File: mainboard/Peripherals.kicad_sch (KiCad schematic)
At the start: 37 parts, among them IC1101 PCAL6416AHF, IC1102 TMP117xxYBG, IC1103 PCA9306JK, IC1104 PCA9633DP1,118, IC1105 RV-8263-C8, Q1101 DMN2053UQ, Q1102 DMN2053UQ

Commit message: Feature: Issue #18
- Replace XPGDWT-BS-0000-00Q2E with XPGDWT-BS-0000-00P5E
- Update CHANGELOG with previous commits

Closes: #18

Signed-off-by: Daniel Kampert <DanielKampert@kampis-elektroecke.de>

Signed-off-by: Daniel Kampert <DanielKampert@kampis-elektroecke.de>
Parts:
- D1101, D1102: manf# XPGDWT-BS-0000-00Q2E -> XPGDWT-BS-0000-00P5E; mouser# 941-PGDWTBS000000Q2E -> 941-XPGDWT-BS-0000-00P5E
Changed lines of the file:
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@@
 			)
 		)
-		(property "manf#" "XPGDWT-BS-0000-00Q2E"
+		(property "manf#" "XPGDWT-BS-0000-00P5E"
 			(at 187.96 102.87 0)
 			(effects
@@
 			)
 		)
-		(property "mouser#" "941-PGDWTBS000000Q2E"
+		(property "mouser#" "941-XPGDWT-BS-0000-00P5E"
 			(at 187.96 102.87 0)
 			(effects
@@
 			)
 		)
-		(property "manf#" "XPGDWT-BS-0000-00Q2E"
+		(property "manf#" "XPGDWT-BS-0000-00P5E"
 			(at 227.33 102.87 0)
 			(effects
@@
 			)
 		)
-		(property "mouser#" "941-PGDWTBS000000Q2E"
+		(property "mouser#" "941-XPGDWT-BS-0000-00P5E"
 			(at 227.33 102.87 0)
 			(effects

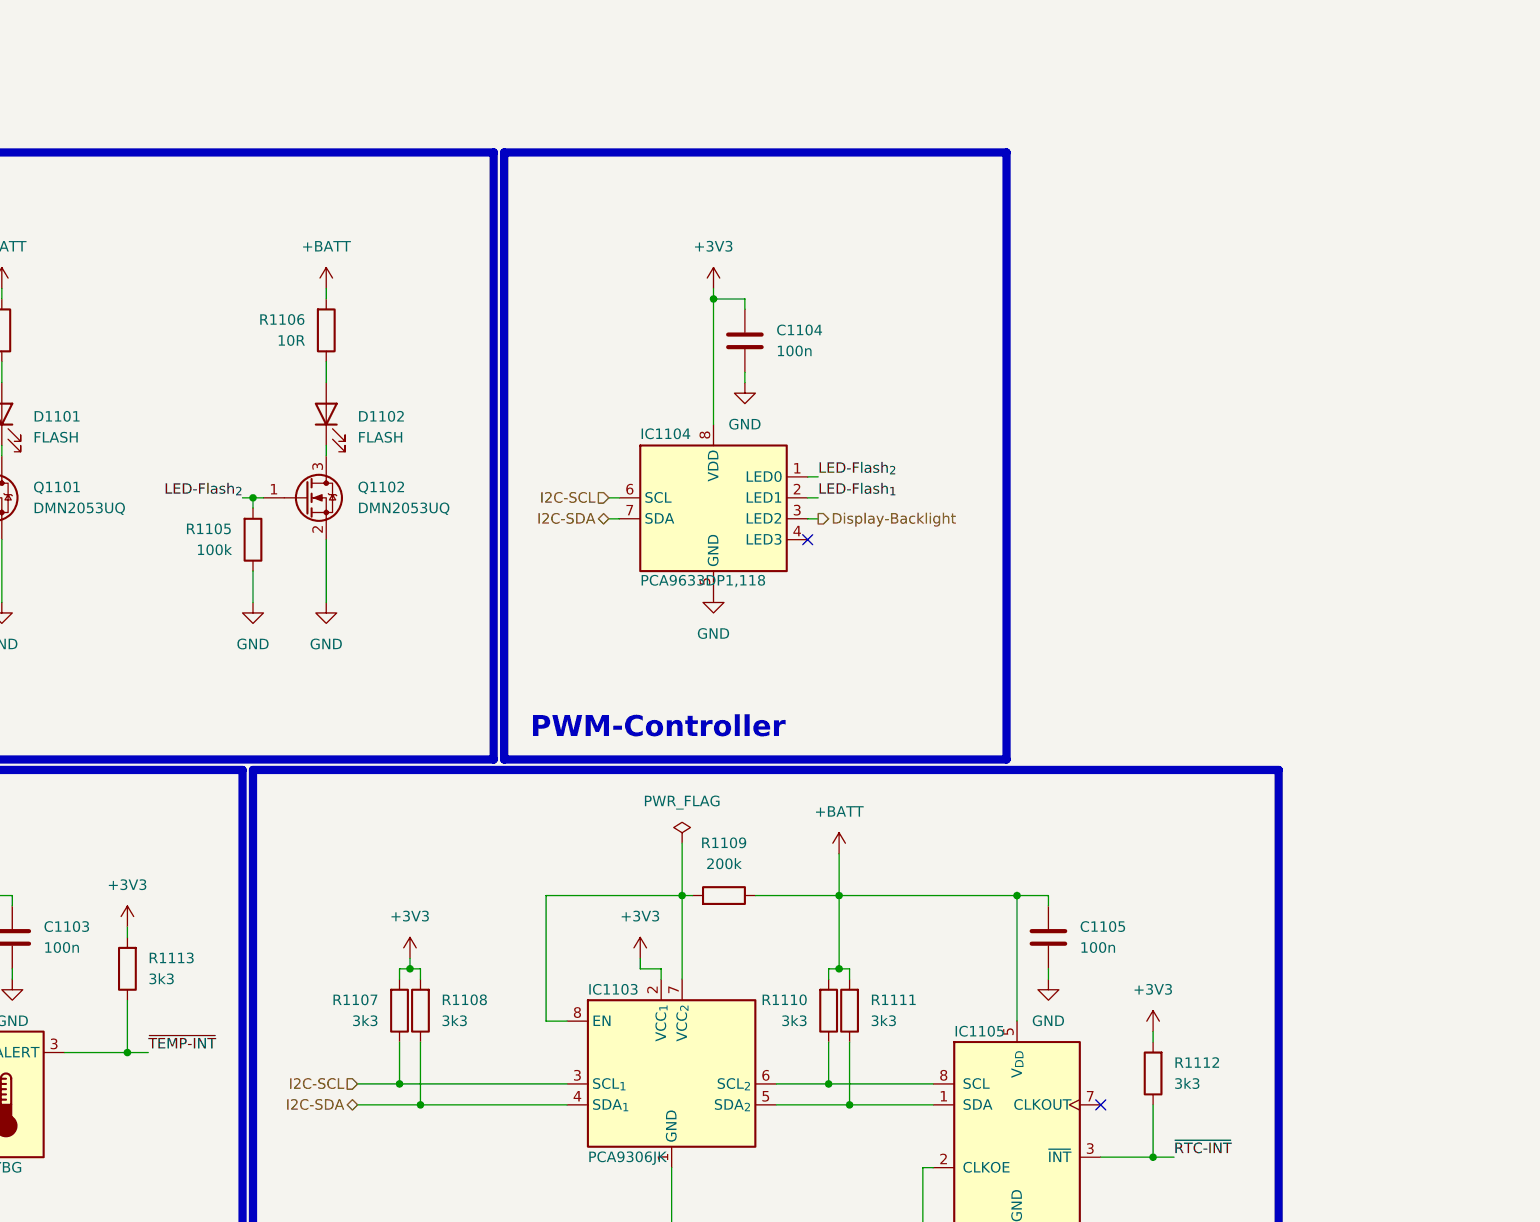
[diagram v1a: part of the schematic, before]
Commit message: Add VL53L1X ToF sensor
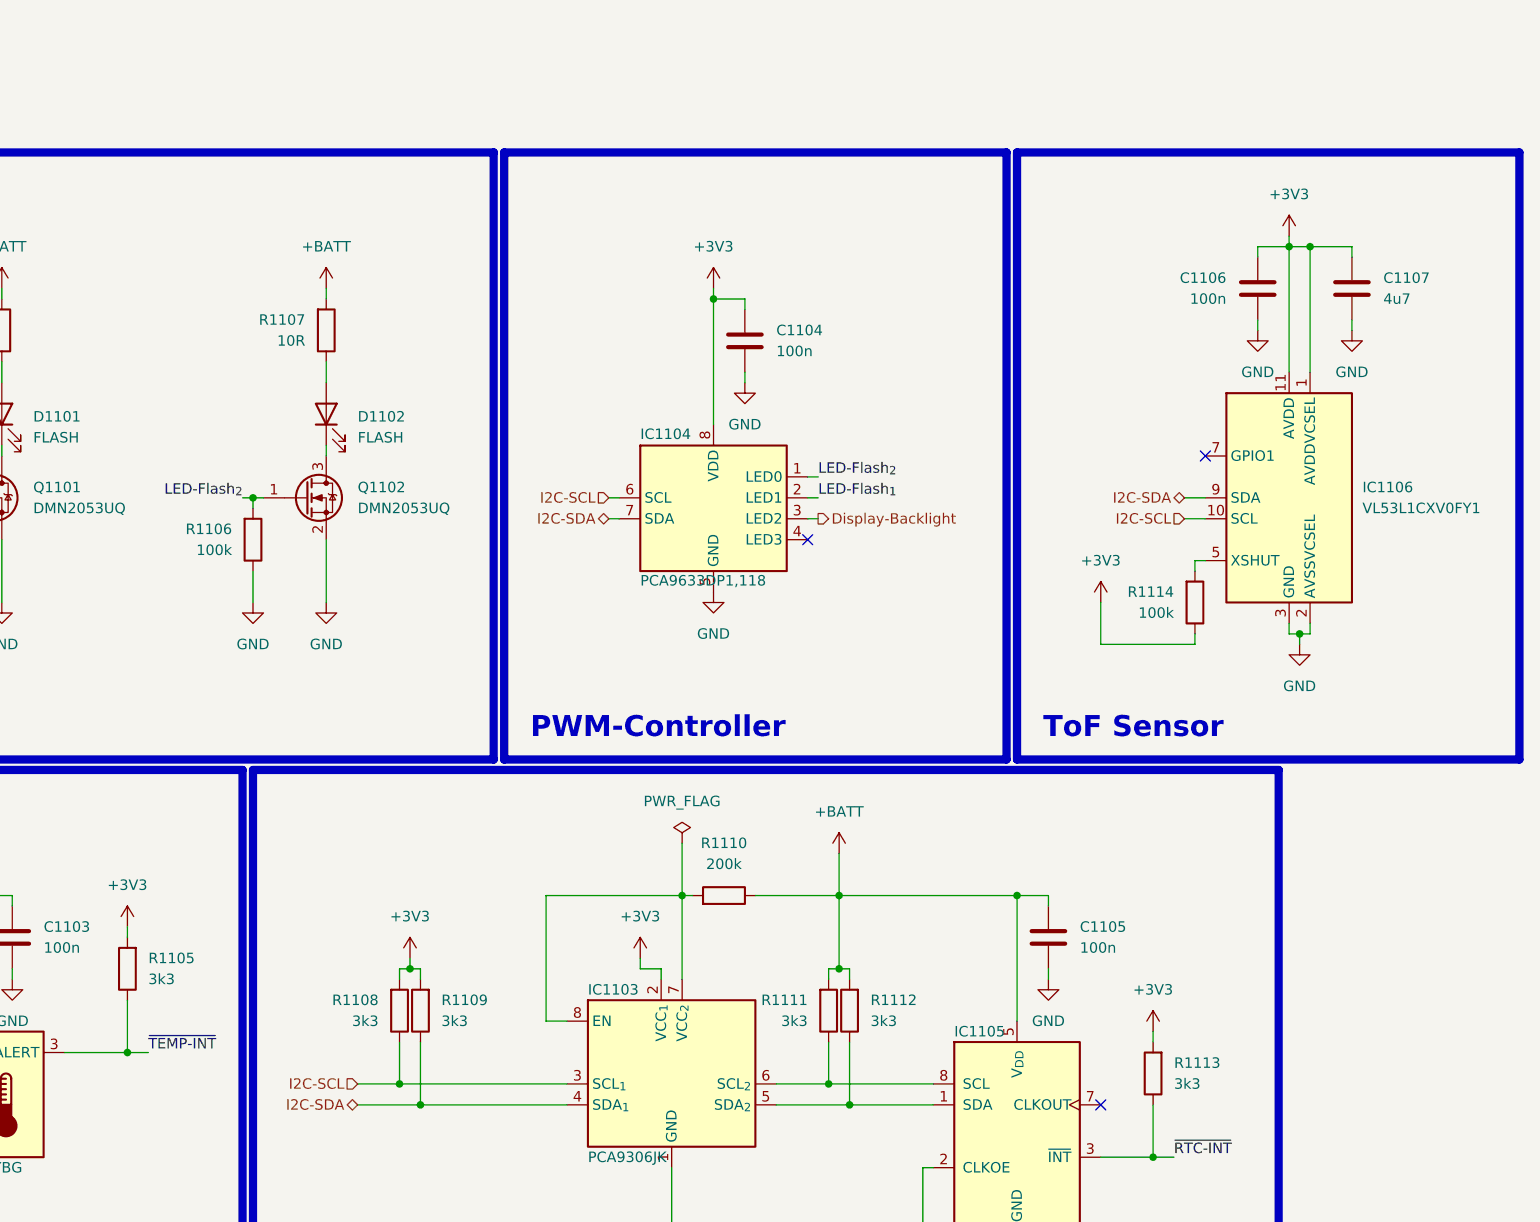
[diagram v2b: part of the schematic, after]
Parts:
- added C1106: 100n, Capacitor_SMD:C_0603_1608Metric, symbol Device:C
- added C1107: 4u7, Capacitor_SMD:C_0603_1608Metric, symbol Device:C
- added IC1106: VL53L1CXV0FY1, Sensor_Distance:ST_VL53L1x, symbol Sensor_Distance:VL53L1CXV0FY1
- added R1114: 100k, Resistor_SMD:R_0603_1608Metric, symbol Device:R
- renumbered R1113 to R1105, R1105 to R1106, R1106 to R1107, R1107 to R1108, R1108 to R1109, R1109 to R1110, R1110 to R1111, R1111 to R1112, R1112 to R1113
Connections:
- net +3V3: now also C1106.1, C1107.1, IC1106.1 (AVDDVCSEL), IC1106.11 (AVDD), R1114.1
- net GND: now also C1106.2, C1107.2, IC1106.12 (GND), IC1106.2 (AVSSVCSEL), IC1106.3 (GND), IC1106.4 (GND), IC1106.6 (GND)
- net I2C-SCL: now also IC1106.10 (SCL)
- net I2C-SDA: now also IC1106.9 (SDA)
- new net: IC1106.5 (XSHUT), R1114.2
- no-connect marks 8 -> 9

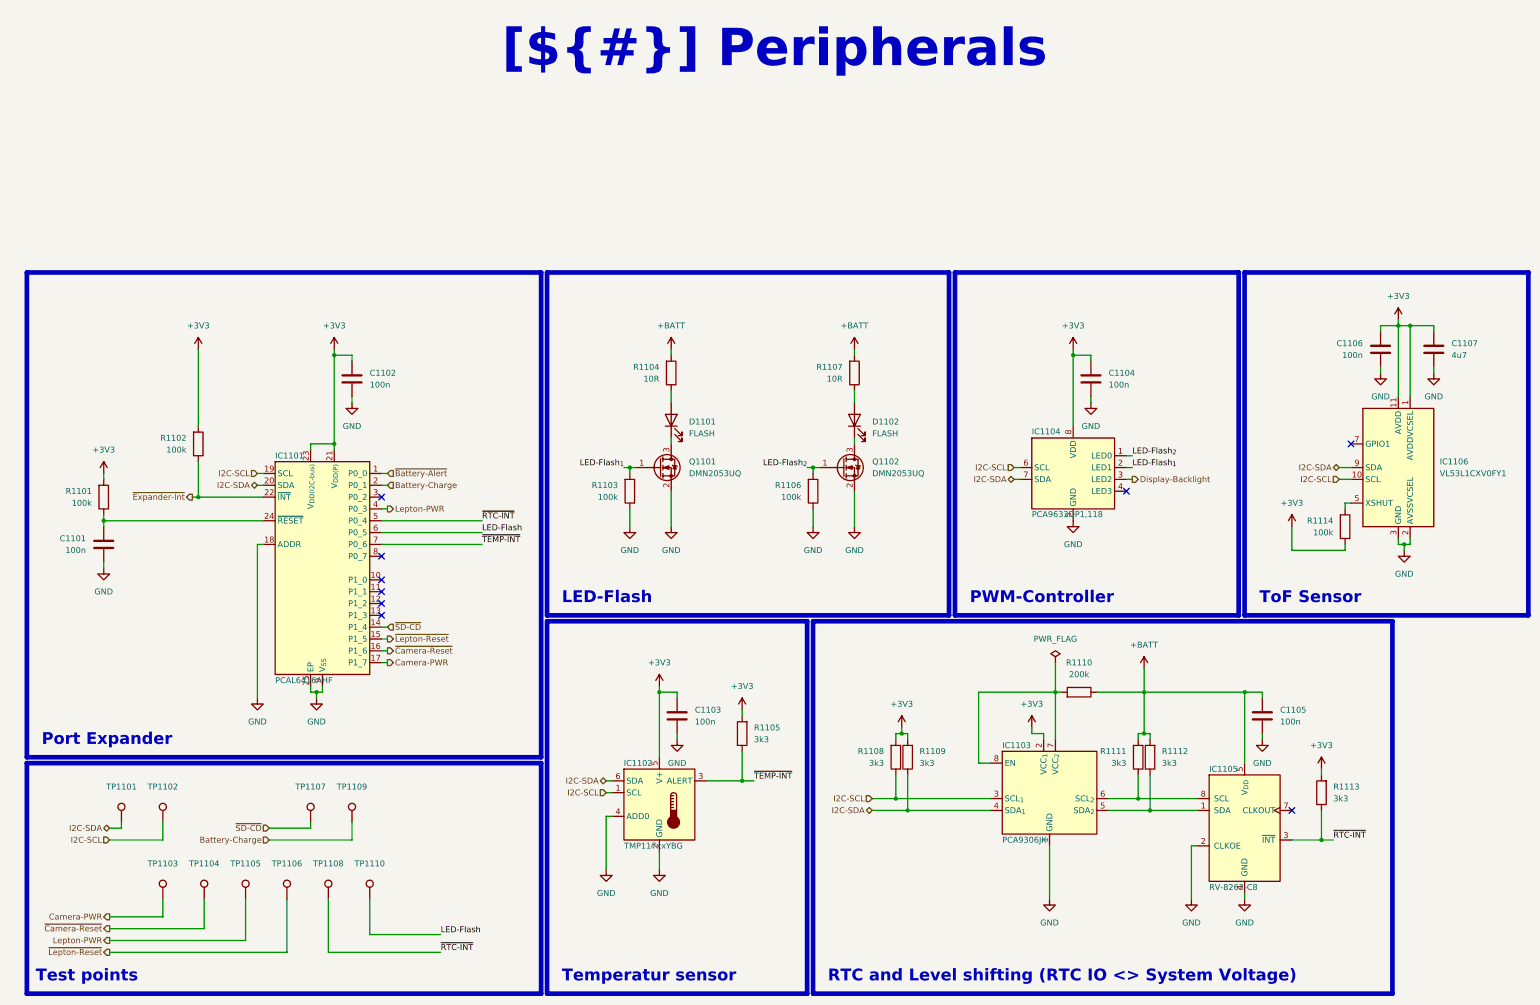
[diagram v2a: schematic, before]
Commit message: Changed: Fix different minor assembly ToDos
Signed-off-by: Daniel Kampert <DanielKampert@kampis-elektroecke.de>
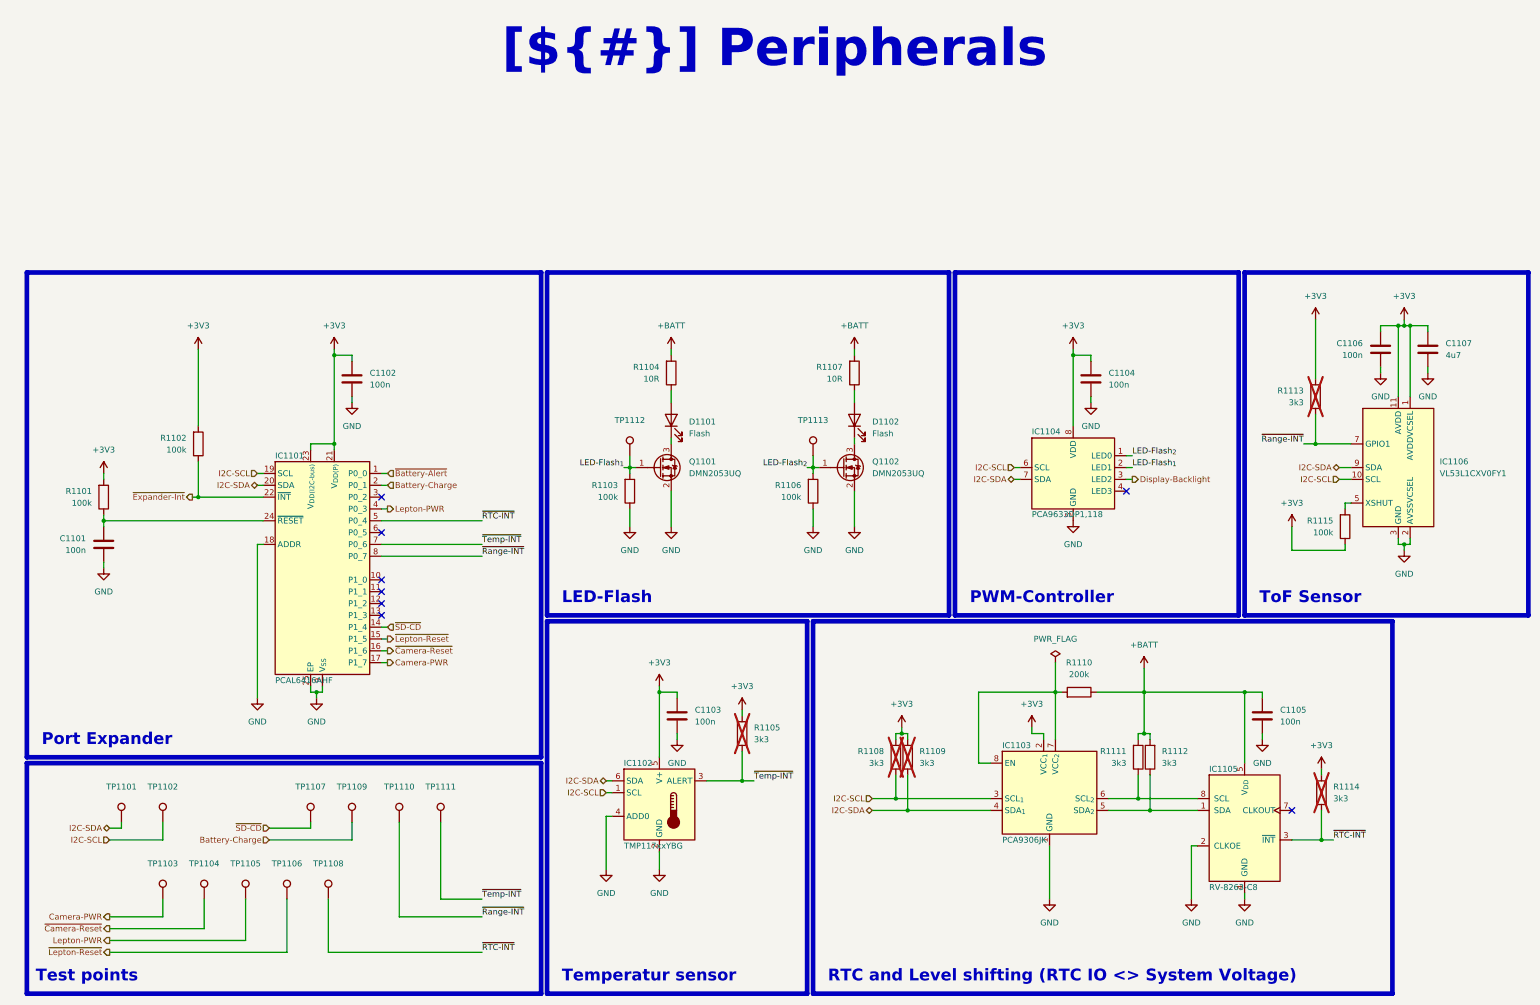
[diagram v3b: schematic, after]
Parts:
- added R1113: 3k3, Resistor_SMD:R_0603_1608Metric, symbol Device:R
- added TP1111, TP1112, TP1113: ~, Testpoints_Kampi:TestPoint_Pad_1.0x1.0mm, symbol Connector:TestPoint
- C1107: manf# 06033D475KAT2A -> 06036D475MAT4A; mouser# 581-06033D475KAT2A -> 581-06036D475MAT4A
- D1101, D1102: value FLASH -> Flash
- R1105, R1108, R1109: now not fitted; now left out of the parts list
- R1114: renamed from R1113; now not fitted; now left out of the parts list
- renumbered R1114 to R1115
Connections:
- net +3V3: now also R1113.2
- net LED-Flash_{1}: now also TP1112.1
- net LED-Flash_{2}: now also TP1113.1
- net ~{Range-INT}: now reaches IC1106.7 (GPIO1)
- net ~{Range-INT}: now also IC1101.8 (P0_7), TP1110.1, R1113.1
- net LED-Flash: no longer names the net of IC1101.6 (P0_5)
- net LED-Flash: no longer TP1110.1
- net ~{TEMP-INT} renamed ~{Temp-INT}
- net ~{Temp-INT}: now also TP1111.1
- no-connect marks 9 -> 8
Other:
- moved on the sheet: C1107

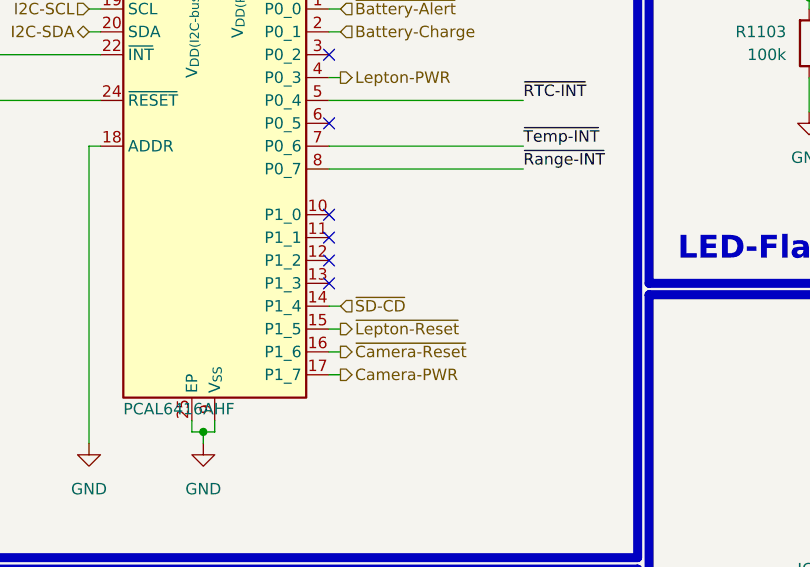
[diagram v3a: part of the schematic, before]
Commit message: Removed: Remove camera PWD signal from camera power supply enable
- The camera PWD signal is now used as a separate signal
- Solves incompatible signal levels for both enable pins
- Fix DRC issues

Signed-off-by: Daniel Kampert <DanielKampert@kampis-elektroecke.de>
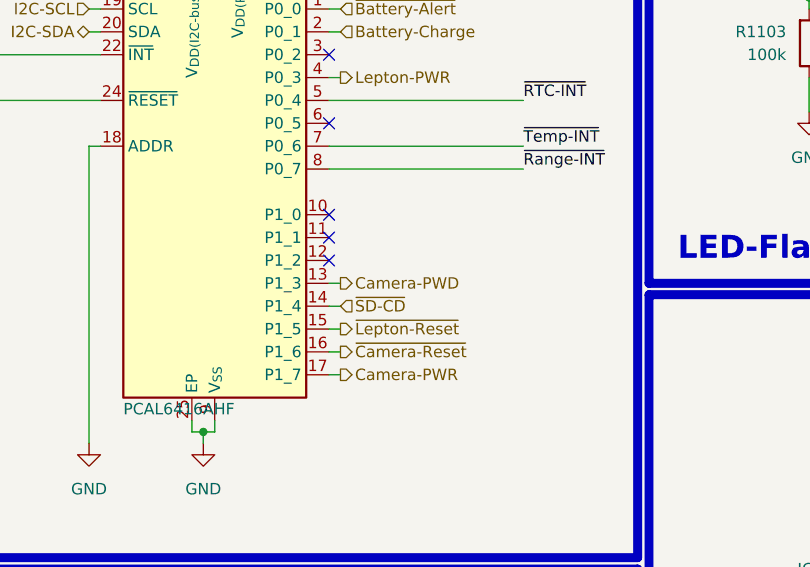
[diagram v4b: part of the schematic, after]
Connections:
- net Camera-PWD: now reaches IC1101.13 (P1_3)
- no-connect marks 8 -> 7
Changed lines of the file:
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@@
-	)
-	(no_connect
-		(at 125.73 144.78)
 	)
 	(no_connect
@@
 		(pts
 			(xy 289.56 161.29) (xy 311.15 161.29)
+		)
+		(stroke
+			(width 0)
+			(type default)
+		)
+	)
+	(wire
+		(pts
+			(xy 125.73 144.78) (xy 127 144.78)
 		)
 		(stroke
@@
 		(effects
 			(font
+				(size 1.27 1.27)
+			)
+			(justify left)
+		)
+	)
+	(hierarchical_label "Camera-PWD"
+		(shape output)
+		(at 127 144.78 0)
+		(effects
+			(font

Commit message: Update to KiCad 10
Closes: #31, #29, #27

Signed-off-by: Daniel Kampert <DanielKampert@kampis-elektroecke.de>
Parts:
- TP1101, TP1102, TP1103, TP1104, TP1105, TP1106, TP1107, TP1108, TP1109, TP1110, TP1111, TP1112, TP1113: value ~ -> (none)
